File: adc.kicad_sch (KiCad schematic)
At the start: 13 parts, among them U7 MCP3008

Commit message: unsplit grounds, finish power circuitry, start picking footprints/partnumbers
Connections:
- net GNDD is gone; now on net GND: U7.9 (DGND)
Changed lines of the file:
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@@
 		(in_pos_files yes)
 		(dnp no)
-		(property "Reference" "#PWR032"
+		(property "Reference" "#PWR32"
 			(at 104.14 142.24 0)
 			(hide yes)
@@
 			(project "pbx-sniffer-v2"
 				(path "/eb421281-26a1-483f-b39a-0425ec8eb8df/ff2bf5b0-8d55-4ab2-beca-8dca5e42da3e"
-					(reference "#PWR032")
+					(reference "#PWR32")
 					(unit 1)
 				)
@@
 	)
 	(symbol
-		(lib_id "power:GNDD")
+		(lib_id "power:GND")
 		(at 111.76 135.89 0)
 		(unit 1)
@@
 		(in_pos_files yes)
 		(dnp no)
-		(fields_autoplaced yes)
-		(property "Reference" "#PWR033"
+		(property "Reference" "#PWR33"
 			(at 111.76 142.24 0)
 			(hide yes)
@@
 			)
 		)
-		(property "Value" "GNDD"
+		(property "Value" "GND"
 			(at 111.76 139.7 0)
 			(show_name no)
@@
 			)
 		)
-		(property "Description" "Power symbol creates a global label with name \"GNDD\" , digital ground"
+		(property "Description" "Power symbol creates a global label with name \"GND\" , ground"
 			(at 111.76 135.89 0)
 			(hide yes)
@@
 			(project "pbx-sniffer-v2"
 				(path "/eb421281-26a1-483f-b39a-0425ec8eb8df/ff2bf5b0-8d55-4ab2-beca-8dca5e42da3e"
-					(reference "#PWR033")
-					(unit 1)
-				)
+					(reference "#PWR33")
+					(unit 1)
+				)

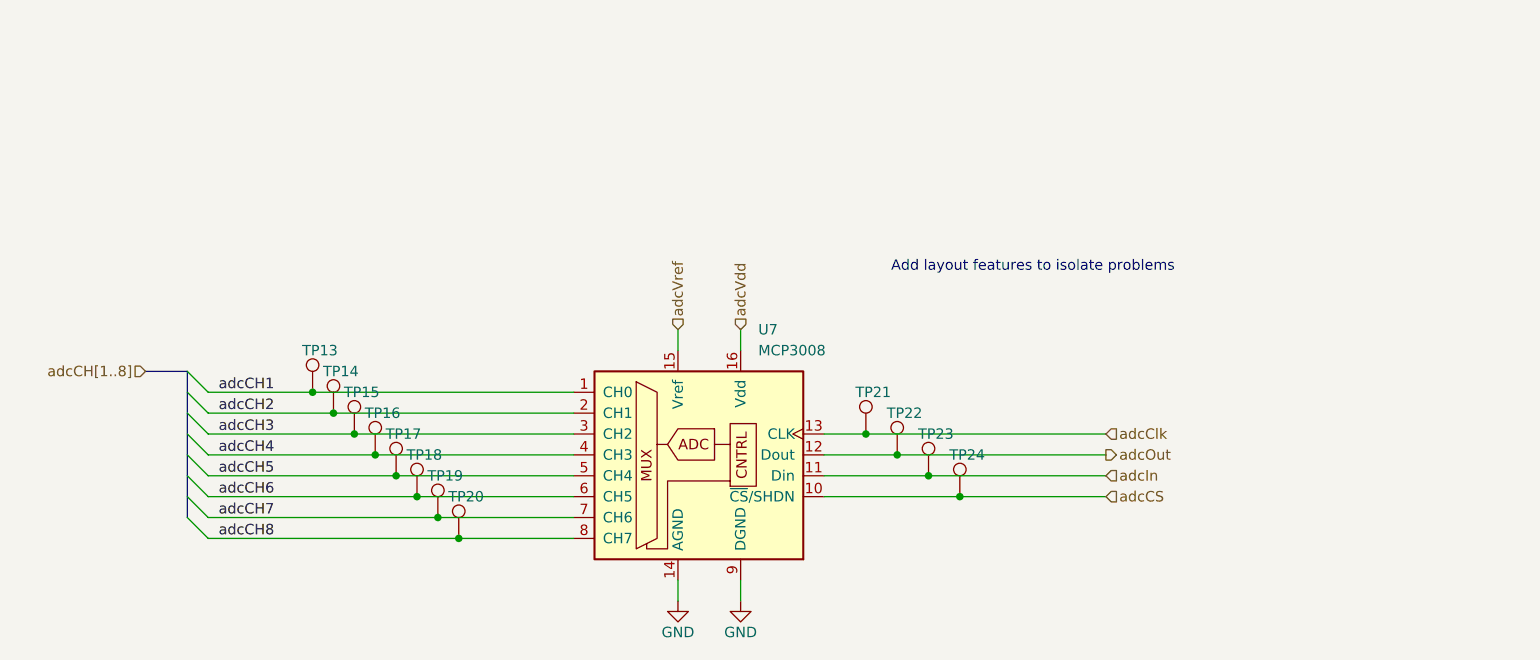
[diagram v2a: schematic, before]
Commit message: added power mux, finished up schematic and picking footprints/partnumbers
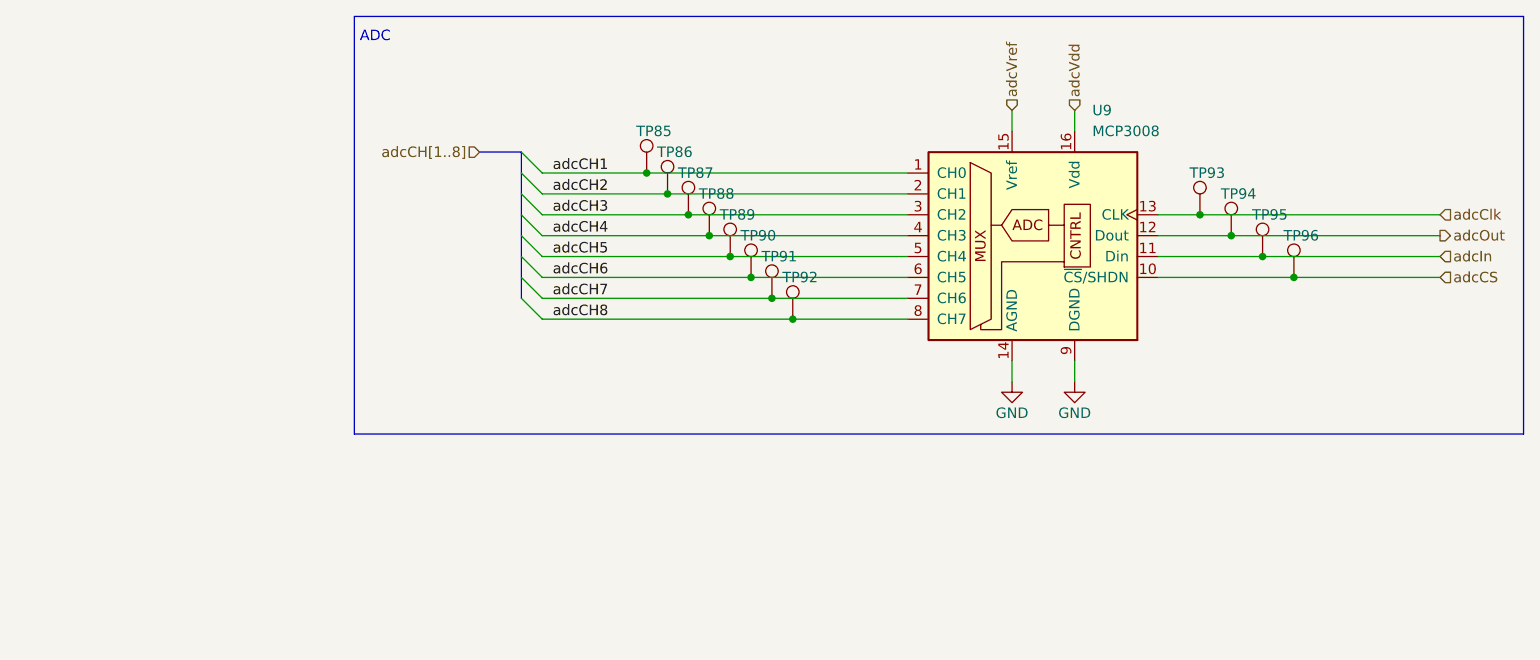
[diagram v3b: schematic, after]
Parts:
- U9: renamed from U7; footprint Package_DIP:DIP-16_W7.62mm -> Package_SO:SOIC-16_3.9x9.9mm_P1.27mm; DKPN MCP3008-I/P-ND -> MCP3008-I/SL-ND
- renumbered TP13 to TP85, TP14 to TP86, TP15 to TP87, TP16 to TP88, TP17 to TP89, TP18 to TP90, TP19 to TP91, TP20 to TP92, TP21 to TP93, TP22 to TP94, TP23 to TP95, TP24 to TP96
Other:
- note added: "ADC"
- note removed: "Add layout features to isolate problems"
- moved on the sheet: TP85, TP86, TP87, TP88, TP89, TP90, TP91, TP92, TP93, TP94, TP95, TP96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

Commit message: nearly complete layout lol
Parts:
- removed TP96: TestPoint, Testpoints:M5_3in1_TestPoint, symbol Connector:TestPoint
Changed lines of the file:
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@@
-	)
-	(junction
-		(at 179.07 96.52)
-		(diameter 0)
-		(color 0 0 0 0)
 	)
 	(junction
@@
 	(wire
 		(pts
-			(xy 179.07 96.52) (xy 196.85 96.52)
+			(xy 162.56 96.52) (xy 196.85 96.52)
 		)
 		(stroke
@@
 		(pts
 			(xy 87.63 99.06) (xy 115.57 99.06)
-		)
-		(stroke
-			(width 0)
-			(type default)
-		)
-	)
-	(wire
-		(pts
-			(xy 162.56 96.52) (xy 179.07 96.52)
 		)
 		(stroke
@@
 					(unit 1)
 				)
-			)
-		)
-	)
-	(symbol
-		(lib_id "Connector:TestPoint")
-		(at 179.07 96.52 0)
-		(unit 1)
-		(body_style 1)
-		(exclude_from_sim no)
-		(in_bom yes)
-		(on_board yes)
-		(in_pos_files yes)
-		(dnp no)
-		(property "Reference" "TP96"
-			(at 177.8 91.44 0)
-			(show_name no)
-			(do_not_autoplace no)
-			(effects
-				(font
-					(size 1.27 1.27)
-				)
-				(justify left)
-			)
-		)
-		(property "Value" "TestPoint"
-			(at 181.61 94.4879 0)
-			(hide yes)
-			(show_name no)
-			(do_not_autoplace no)
-			(effects
-				(font
-					(size 1.27 1.27)
-				)
-				(justify left)
-			)
-		)
-		(property "Footprint" "Testpoints:M5_3in1_TestPoint"
-			(at 184.15 96.52 0)
-			(hide yes)
-			(show_name no)
-			(do_not_autoplace no)
-			(effects
-				(font
-					(size 1.27 1.27)
-				)
-			)
-		)
-		(property "Datasheet" ""
-			(at 184.15 96.52 0)
-			(hide yes)
-			(show_name no)
-			(do_not_autoplace no)
-			(effects
-				(font
-					(size 1.27 1.27)
-				)
-			)
-		)
-		(property "Description" "test point"
-			(at 179.07 96.52 0)
-			(hide yes)
-			(show_name no)
-			(do_not_autoplace no)
-			(effects
-				(font
-					(size 1.27 1.27)
-				)
-			)
-		)
-		(pin "1"
-		)
-		(instances
-			(project "pbx-sniffer-v2"
-				(path "/eb421281-26a1-483f-b39a-0425ec8eb8df/ff2bf5b0-8d55-4ab2-beca-8dca5e42da3e"
-					(reference "TP96")
-					(unit 1)
-				)
